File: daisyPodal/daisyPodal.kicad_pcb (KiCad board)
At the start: 2 copper layers, 76 x 86 mm, 45 parts, among them J1 Guitar in, J2 Left out, J3 fsw pin 1, J4 fsw pin 4, J5 fsw pin 6, J6 fsw pin 3, J7 fsw pin 2, J8 fsw pin 5, SW1 Switch 1, SW2 Switch 2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

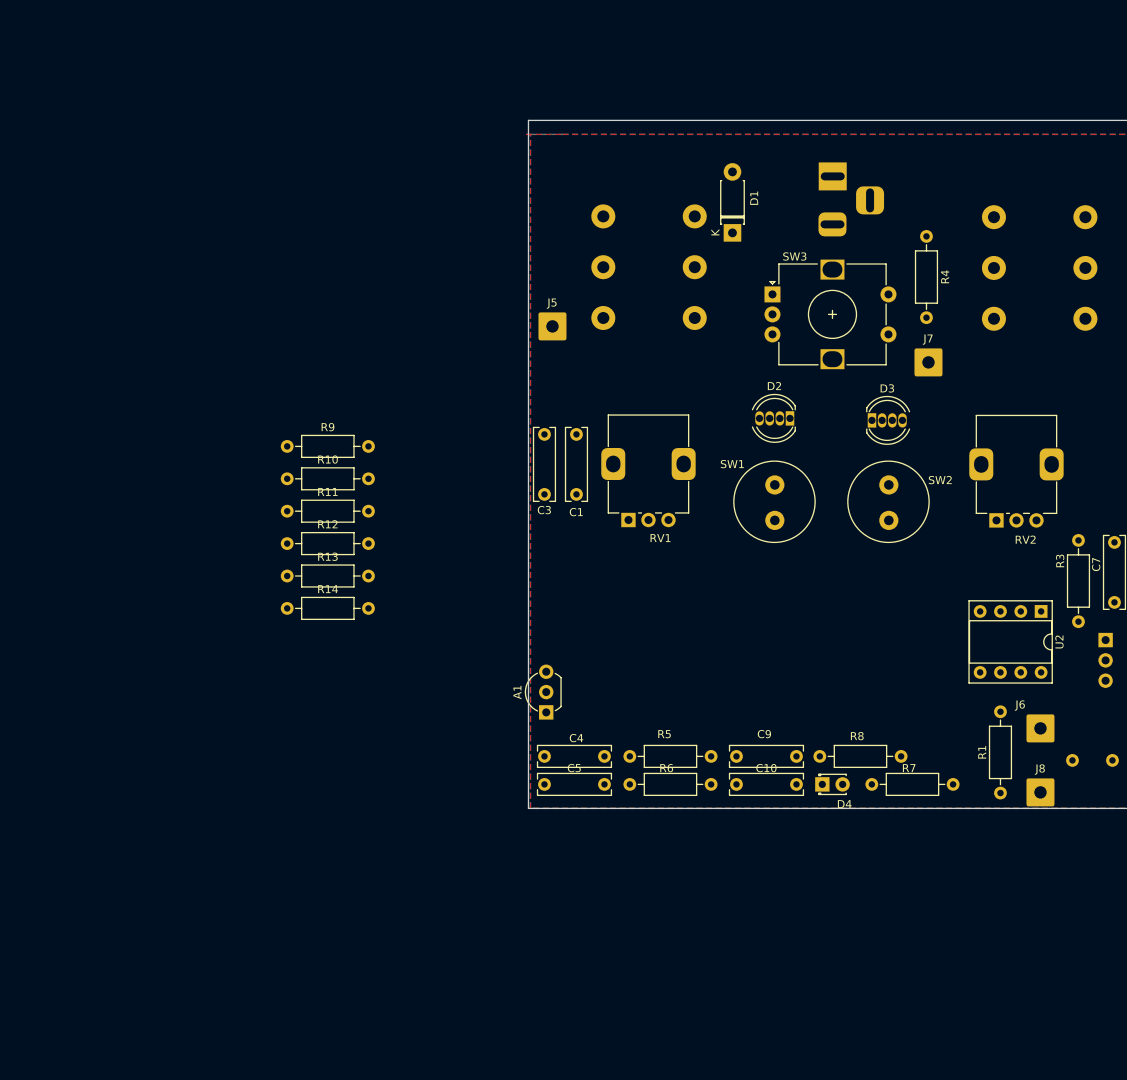
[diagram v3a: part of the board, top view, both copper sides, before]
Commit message: Add right out - stereo now
Replaced TL072 with TL074
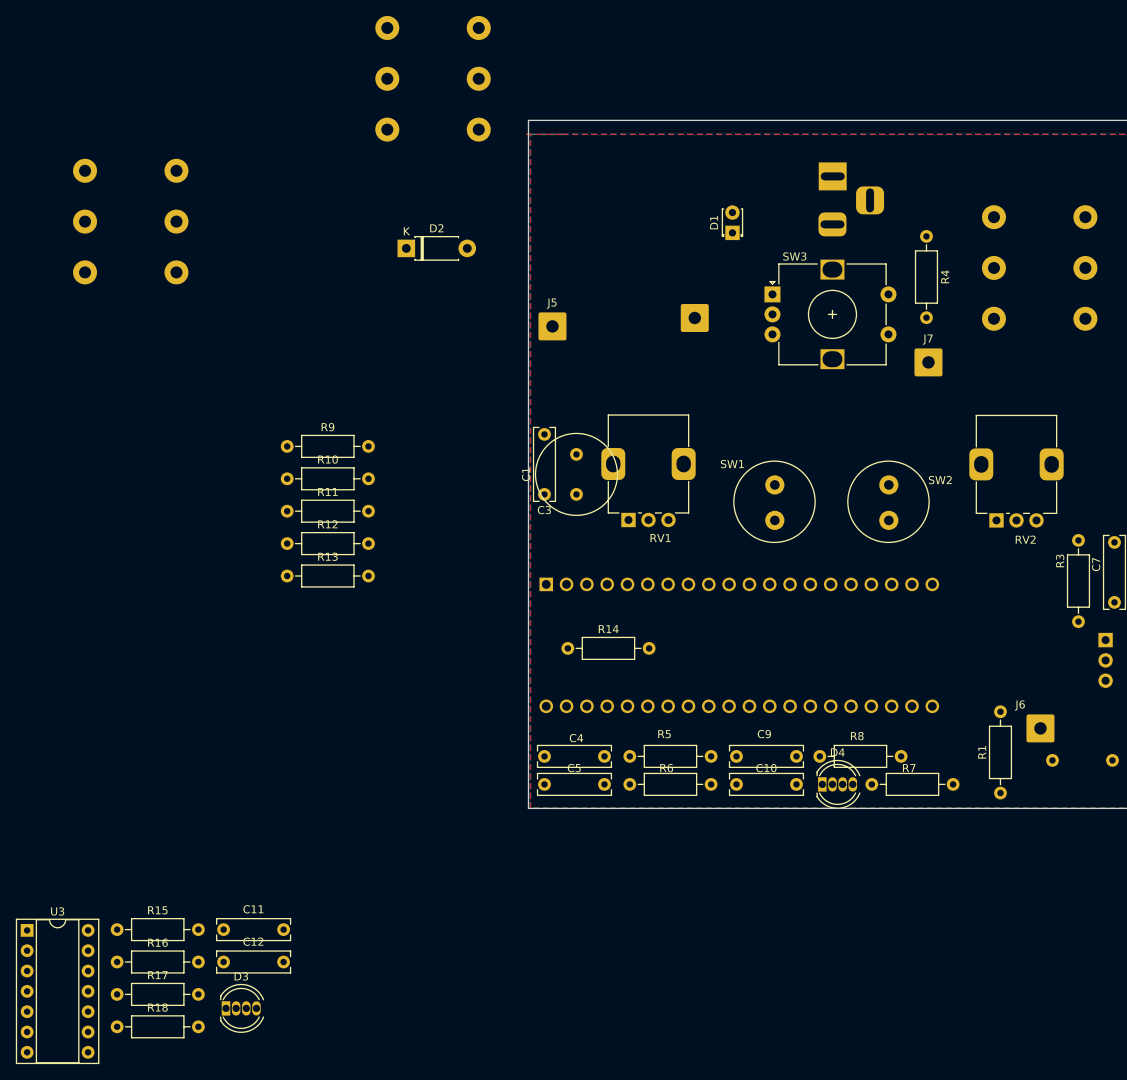
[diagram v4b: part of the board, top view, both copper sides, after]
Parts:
- removed U2: TL072, Package_DIP:DIP-8_W7.62mm_Socket
- added C11: 1u, Capacitor_THT:C_Rect_L9.0mm_W2.5mm_P7.50mm_MKT, F.Cu at (61.9, 137.2)
- added C12: 1u, Capacitor_THT:C_Rect_L9.0mm_W2.5mm_P7.50mm_MKT, F.Cu at (61.9, 141.2)
- added J10: Right out, Connector_Audio:Jack_6.35mm_Neutrik_NRJ6HM-1_Horizontal, B.Cu at (56.0, 55.0)
- added R15: 1M, Resistor_THT:R_Axial_DIN0207_L6.3mm_D2.5mm_P10.16mm_Horizontal, F.Cu at (48.6, 137.2)
- added R16: 1M, Resistor_THT:R_Axial_DIN0207_L6.3mm_D2.5mm_P10.16mm_Horizontal, F.Cu at (48.6, 141.2)
- added R17: 100R, Resistor_THT:R_Axial_DIN0207_L6.3mm_D2.5mm_P10.16mm_Horizontal, F.Cu at (48.6, 145.2)
- added R18: 100K, Resistor_THT:R_Axial_DIN0207_L6.3mm_D2.5mm_P10.16mm_Horizontal, F.Cu at (48.6, 149.3)
- added U3: TL074, Package_DIP:DIP-14_W7.62mm_Socket, F.Cu at (37.3, 137.2)
- A1: footprint Package_TO_SOT_THT:TO-92_Inline_Wide_78L05_dc -> Module:Electrosmith_Daisy_Seed; moved to B.Cu
- C1: value 100n -> 100u; footprint Capacitor_THT:C_Rect_L9.0mm_W2.5mm_P7.50mm_MKT -> Capacitor_THT:C_Radial_D10.0mm_H16.0mm_P5.00mm
- C2: value 100u -> 100p; footprint Capacitor_THT:C_Radial_D10.0mm_H16.0mm_P5.00mm -> Capacitor_THT:C_Rect_L9.0mm_W2.5mm_P7.50mm_MKT
- C3: value 100n -> 1u
- C6: value 100p -> 1n
- C7: value 1n -> 100n
- C8: value 1u -> 100n
- D1: value 1N5819 -> LED; footprint Diode_THT:D_DO-41_SOD81_P7.62mm_Horizontal -> LED_THT:LED_D1.8mm_W3.3mm_H2.4mm
- D2: value LED 1 -> 1N5819; footprint LED_THT:LED_D5.0mm-4_RGB -> Diode_THT:D_DO-41_SOD81_P7.62mm_Horizontal
- D3: value LED 2 -> LED_RAGB
- D4: value LED -> LED_RAGB; footprint LED_THT:LED_D1.8mm_W3.3mm_H2.4mm -> LED_THT:LED_D5.0mm-4_RGB
- J2: value Left out -> fsw pin 1; footprint Connector_Audio:Jack_6.35mm_Neutrik_NRJ6HM-1_Horizontal -> Connector_Wire:SolderWire-0.75sqmm_1x01_D1.25mm_OD3.5mm
- J3: value fsw pin 1 -> fsw pin 2
- J5: value fsw pin 6 -> fsw pin 5
- J6: value fsw pin 3 -> fsw pin 6
- J7: value fsw pin 2 -> fsw pin 3
- J8: value fsw pin 5 -> Left out; footprint Connector_Wire:SolderWire-0.75sqmm_1x01_D1.25mm_OD3.5mm -> Connector_Audio:Jack_6.35mm_Neutrik_NRJ6HM-1_Horizontal; moved to B.Cu
- R1, R2: value 1M -> 1k
- R13: value 1k -> 100R
- R14: value 1k -> 100K
- R3, R4: value 1k -> 1M
- R7: value 100K -> 1k
- R8: value 100R -> 1k
- SW1: value Switch 1 -> Switch 2
- SW2: value Switch 2 -> Switch 1
- moved D3 109.2 mm to (62.2, 147.0)
- moved J8 108.6 mm to (93.8, 37.1), turned to 90 degrees
- moved D2 52.5 mm to (84.7, 52.0), turned to 0 degrees
- moved R14 35.4 mm to (104.9, 102.0)
- moved A1 16.0 mm to (102.2, 94.0), turned to -90 degrees
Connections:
- C1 pad 1: GND -> /VCC
- C1 pad 2: /VCC -> GND
- C10 pad 1: /Left out -> Net-(C10-Pad1)
- C10 pad 2: Net-(U2B-+) -> Net-(J7-Pin_1)
- C2 pad 1: /VCC -> Net-(J4-Pin_1)
- C3 pad 1: GND -> Net-(J4-Pin_1)
- C3 pad 2: /VCC -> Net-(C3-Pad2)
- C4 pad 2: +5V -> /VCC
- C5 pad 2: +5V -> /VCC
- C6 pad 1: Net-(J4-Pin_1) -> Net-(U3A-+)
- C7 pad 1: Net-(U2A-+) -> GND
- C7 pad 2: GND -> +5V
- C8 pad 1: Net-(J4-Pin_1) -> GND
- C8 pad 2: Net-(C8-Pad2) -> +5V
- C9 pad 1: Net-(C9-Pad1) -> /Left out
- C9 pad 2: Net-(J6-Pin_1) -> Net-(U3B-+)
- D1 pad 1: /VCC -> Net-(D1-K)
- D1 pad 2: Net-(BT1-+) -> Net-(D1-A)
- D2 pad 1: /LED_1_G -> /VCC
- D2 pad 2: /LED_1_B -> Net-(BT1-+)
- D3 pad 1: /LED_2_G -> Net-(D3-RK)
- D3 pad 2: /LED_2_B -> /3v3
- D3 pad 3: GND -> Net-(D3-GK)
- D3 pad 4: /LED_2_R -> Net-(D3-BK)
- D4 pad 1: Net-(D4-K) -> Net-(D4-RK)
- D4 pad 2: Net-(D4-A) -> /3v3
- J1 pad T: Net-(J3-Pin_1) -> Net-(J2-Pin_1)
- J3 pad 1: Net-(J3-Pin_1) -> Net-(D1-K)
- J5 pad 1: Net-(J5-Pin_1) -> GND
- J7 pad 1: Net-(D4-K) -> Net-(J7-Pin_1)
- R1 pad 1: +5V -> Net-(BT1-+)
- R1 pad 2: Net-(U2A-+) -> Net-(D1-A)
- R10 pad 1: /LED_1_G -> /LED_2_B
- R10 pad 2: Net-(D7-GK) -> Net-(D4-RK)
- R11 pad 1: /LED_1_R -> /LED_2_G
- R11 pad 2: Net-(D7-BK) -> Net-(D4-GK)
- R12 pad 1: /LED_2_B -> /LED_2_R
- R12 pad 2: Net-(D2-RK) -> Net-(D4-BK)
- R13 pad 1: /LED_2_G -> Net-(U3B--)
- R13 pad 2: Net-(D2-GK) -> Net-(C10-Pad1)
- R14 pad 1: /LED_2_R -> Net-(J7-Pin_1)
- R14 pad 2: Net-(D2-BK) -> GND
- R2 pad 1: Net-(U2A-+) -> Net-(C3-Pad2)
- R2 pad 2: GND -> Net-(U3A-+)
- R3 pad 1: Net-(C8-Pad2) -> +5V
- R3 pad 2: Net-(U2A-+) -> Net-(U3A-+)
- R4 pad 1: Net-(BT1-+) -> Net-(U3A-+)
- R4 pad 2: Net-(D4-A) -> GND
- R5 pad 2: Net-(U2B-+) -> Net-(U3B-+)
- R6 pad 1: Net-(U2B-+) -> Net-(U3B-+)
- R7 pad 1: Net-(J6-Pin_1) -> /LED_1_B
- R7 pad 2: GND -> Net-(D3-RK)
- R8 pad 1: Net-(U2B--) -> /LED_1_G
- R8 pad 2: Net-(C9-Pad1) -> Net-(D3-GK)
- R9 pad 1: /LED_1_B -> /LED_1_R
- R9 pad 2: Net-(D7-RK) -> Net-(D3-BK)
- SW1 pad 1: Net-(A1-SAI2_FS) -> Net-(A1-SAI2_SCK)
- SW2 pad 1: Net-(A1-SAI2_SCK) -> Net-(A1-SAI2_FS)

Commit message: reduce size of box capacitors to fit caps we use
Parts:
- moved D1 151.2 mm to (29.0, 166.4)
- moved J2 145.0 mm to (265.5, 70.0)
- moved SW2 137.7 mm to (266.5, 150.9)
- moved J7 130.8 mm to (272.5, 112.0)
- moved R4 128.4 mm to (274.5, 80.9)
- moved SW1 117.6 mm to (46.0, 167.4)
- moved BT1 113.9 mm to (251.5, 39.0)
- moved RV1 108.7 mm to (221.0, 92.5)
- moved SW3 94.2 mm to (208.2, 111.0)
- moved D4 91.6 mm to (49.1, 145.5)
- moved C9 86.6 mm to (212.8, 150.5)
- moved J6 86.6 mm to (243.2, 147.0)
- moved R3 86.6 mm to (248.0, 123.5)
- moved R8 86.6 mm to (225.8, 150.5)
- moved RV2 86.6 mm to (237.8, 121.0)
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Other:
- board size 76 x 86 mm -> 76 x 80 mm

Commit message: Place components on PCB in sensible blocks
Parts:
- removed J10: Right out, Connector_Audio:Jack_6.35mm_Neutrik_NRJ6HM-1_Horizontal
- removed U3: TL074, Package_DIP:DIP-14_W7.62mm_Socket
- added J9: fsw pin 3, Connector_Wire:SolderWire-0.75sqmm_1x01_D1.25mm_OD3.5mm, F.Cu at (140.0, 55.0)
- added U2: TL074, Package_DIP:DIP-14_W7.62mm_Socket, F.Cu at (136.9, 106.0)
- C1: moved to B.Cu
- C10, C11, C12, C3, C4, C5, C6, C7, C8, C9: footprint Capacitor_THT:C_Rect_L9.0mm_W2.5mm_P7.50mm_MKT -> Capacitor_THT:C_Rect_L7.0mm_W2.5mm_P5.00mm
- C2: footprint Capacitor_THT:C_Rect_L9.0mm_W2.5mm_P7.50mm_MKT -> Capacitor_THT:C_Rect_L7.0mm_W2.5mm_P5.00mm; moved to F.Cu
- J2: moved to F.Cu
- J7: value fsw pin 3 -> Left out; footprint Connector_Wire:SolderWire-0.75sqmm_1x01_D1.25mm_OD3.5mm -> Connector_Audio:Jack_6.35mm_Neutrik_NRJ6HM-1_Horizontal; moved to B.Cu
- J8: value Left out -> Right out
- R13: value 100R -> 1k
- R14: value 100K -> 1k
- R15, R16: value 1M -> 100R
- R17: value 100R -> 100K
- R7, R8: value 1k -> 1M
- SW1: value Switch 2 -> Switch 1; footprint Button_Switch_THT:SW_CW_GPTS203211B_1 podal -> Connector_Wire:SolderWire-0.75sqmm_1x02_P7mm_D1.25mm_OD3.5mm
- SW2: value Switch 1 -> Switch 2; footprint Button_Switch_THT:SW_CW_GPTS203211B_1 podal -> Connector_Wire:SolderWire-0.75sqmm_1x02_P7mm_D1.25mm_OD3.5mm
- moved J5 153.8 mm to (172.0, 123.0)
- moved J7 146.0 mm to (131.0, 76.0), turned to 90 degrees
- moved J6 133.1 mm to (125.0, 86.0)
- moved D2 130.8 mm to (124.0, 129.0)
- moved J3 126.6 mm to (142.0, 130.0)
- moved D4 119.2 mm to (160.1, 102.0)
- moved R4 119.2 mm to (156.0, 67.8)
- moved R18 117.0 mm to (136.0, 65.0), turned to 90 degrees
- moved R8 115.4 mm to (136.0, 78.0), turned to 90 degrees
- moved D1 115.2 mm to (138.3, 130.0), turned to 180 degrees
- moved R16 114.5 mm to (142.0, 78.0), turned to 90 degrees
- moved R12 113.5 mm to (131.8, 115.0)
- moved SW2 111.7 mm to (157.0, 129.0)
- moved RV1 111.5 mm to (109.5, 95.0)
- moved R13 110.8 mm to (131.8, 118.0)
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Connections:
- C10 pad 1: Net-(C10-Pad1) -> /Left out
- C10 pad 2: Net-(J7-Pin_1) -> Net-(U2B-+)
- C11 pad 1: /Right out -> Net-(C11-Pad1)
- C11 pad 2: Net-(U3C-+) -> Net-(C11-Pad2)
- C6 pad 1: Net-(U3A-+) -> Net-(U2A-+)
- C9 pad 1: /Left out -> /Right out
- J8 pad T: Net-(J6-Pin_1) -> Net-(C11-Pad2)
- R10 pad 1: /LED_2_B -> /LED_1_G
- R10 pad 2: Net-(D4-RK) -> Net-(D3-GK)
- R11 pad 1: /LED_2_G -> /LED_1_R
- R11 pad 2: Net-(D4-GK) -> Net-(D3-BK)
- R12 pad 1: /LED_2_R -> /LED_2_B
- R12 pad 2: Net-(D4-BK) -> Net-(D4-RK)
- R13 pad 1: Net-(U3B--) -> /LED_2_G
- R13 pad 2: Net-(C10-Pad1) -> Net-(D4-GK)
- R14 pad 1: Net-(J7-Pin_1) -> /LED_2_R
- R14 pad 2: GND -> Net-(D4-BK)
- R15 pad 1: +5V -> Net-(U2C--)
- R15 pad 2: Net-(U3C-+) -> Net-(C11-Pad1)
- R16 pad 1: Net-(U3C-+) -> Net-(U2B--)
- R16 pad 2: GND -> Net-(C12-Pad1)
- R17 pad 1: Net-(U3C--) -> Net-(C11-Pad2)
- R17 pad 2: Net-(C12-Pad1) -> GND
- R2 pad 2: Net-(U3A-+) -> Net-(U2A-+)
- R3 pad 2: Net-(U3A-+) -> Net-(R3-Pad2)
- R4 pad 1: Net-(U3A-+) -> Net-(R3-Pad2)
- R7 pad 1: /LED_1_B -> +5V
- R7 pad 2: Net-(D3-RK) -> Net-(U2B-+)
- R8 pad 1: /LED_1_G -> Net-(U2B-+)
- R8 pad 2: Net-(D3-GK) -> GND
- R9 pad 1: /LED_1_R -> /LED_1_B
- R9 pad 2: Net-(D3-BK) -> Net-(D3-RK)
- SW1 pad 1: Net-(A1-SAI2_SCK) -> Net-(A1-SAI2_FS)
- SW2 pad 1: Net-(A1-SAI2_FS) -> Net-(A1-SAI2_SCK)
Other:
- board text added: "Podal v0.2 Denis Crowdy"
- board text removed: "Podal v0.1"

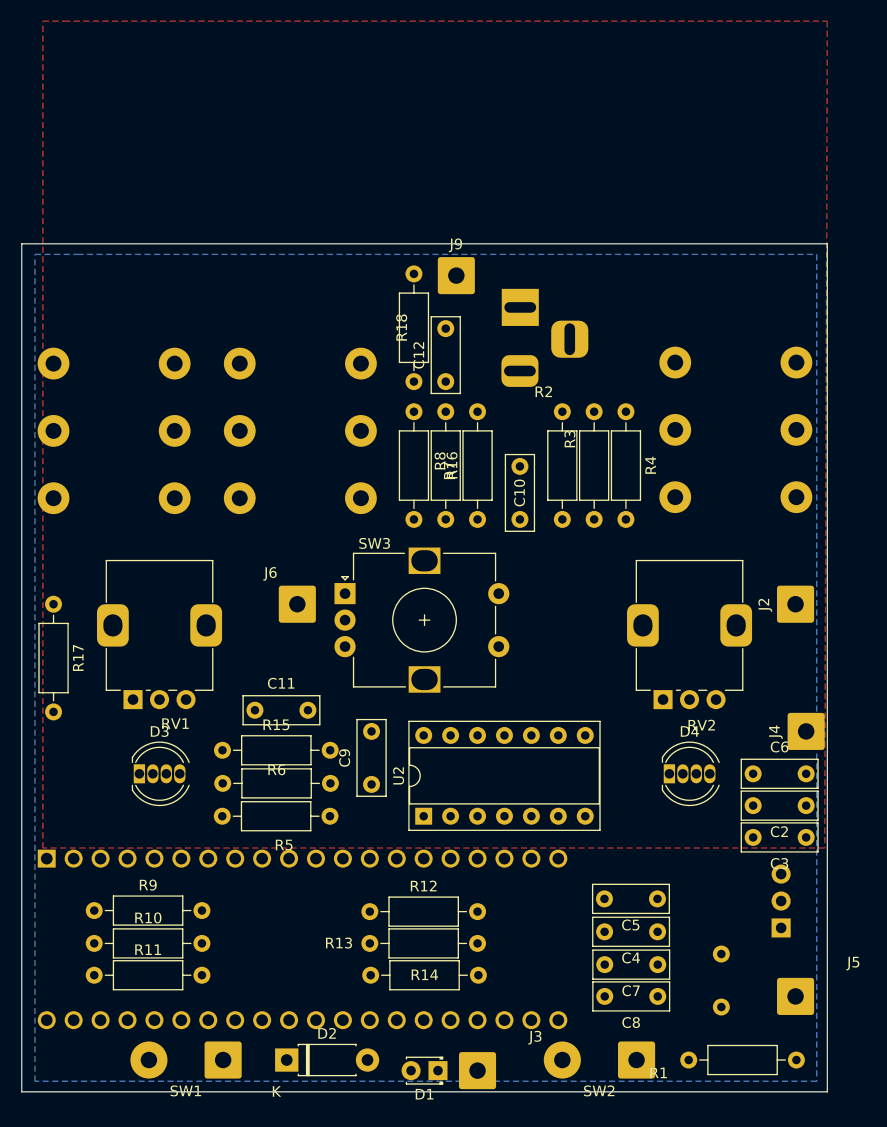
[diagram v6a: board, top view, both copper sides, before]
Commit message: Connect everything together on PCB
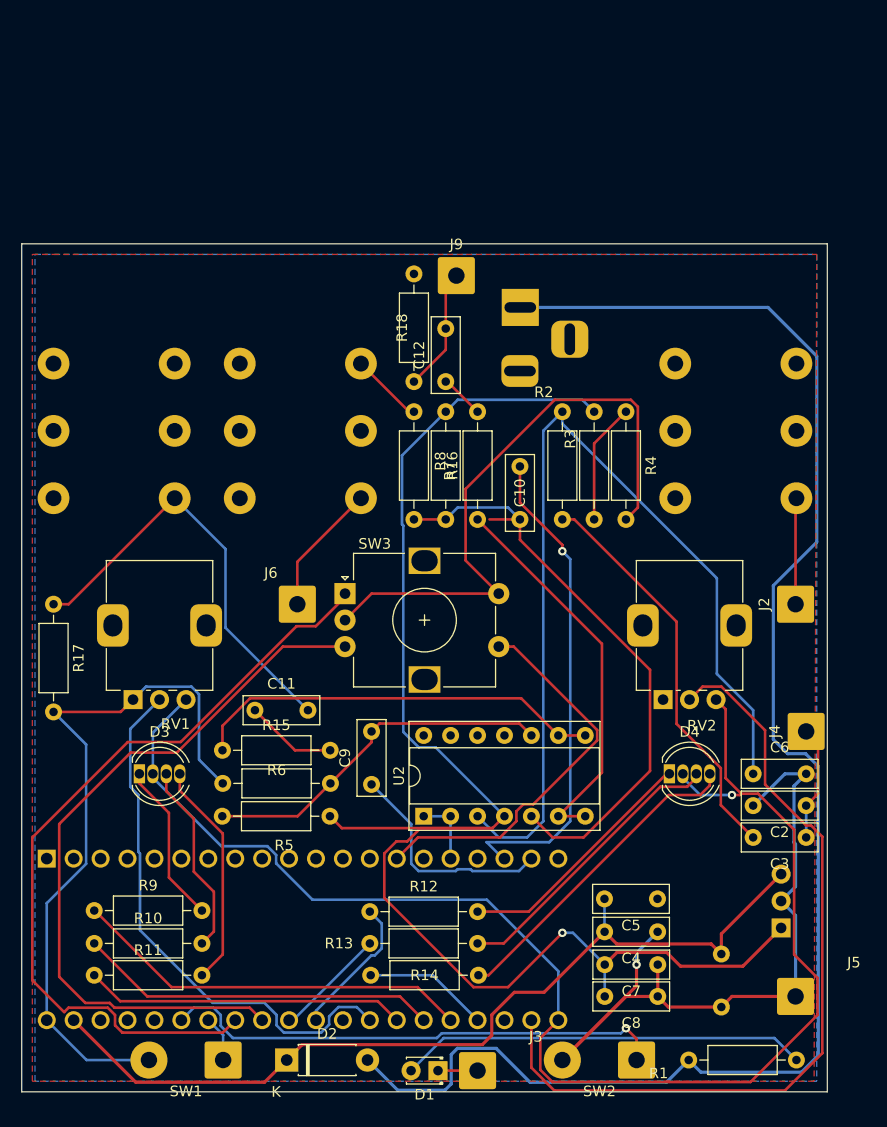
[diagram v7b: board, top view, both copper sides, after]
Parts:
- moved J1 0.10 mm to (172.1, 76.0)
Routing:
- net GND: track 0.00 -> 205.4 mm, vias 0 -> 1
- net Net-(BT1-+): track 0.00 -> 150.6 mm
- net +5V: track 0.00 -> 142.3 mm, vias 0 -> 1
- net /3v3: track 0.00 -> 135.4 mm, vias 0 -> 1
- net Net-(U2A-+): track 0.00 -> 88.7 mm
- net /VCC: track 0.00 -> 84.4 mm
- net Net-(A1-ADC_0): track 0.00 -> 76.6 mm
- net Net-(A1-SAI2_SD_A): track 0.00 -> 75.3 mm
- net Net-(A1-SAI2_SD_B): track 0.00 -> 69.1 mm
- net Net-(U2B-+): track 0.00 -> 57.2 mm
- net Net-(A1-ADC_6): track 0.00 -> 51.5 mm
- net Net-(A1-SAI2_SCK): track 0.00 -> 48.0 mm, vias 0 -> 1
- net /Left out: track 0.00 -> 47.4 mm, vias 0 -> 1
- net Net-(C11-Pad2): track 0.00 -> 40.8 mm
- net Net-(U2C--): track 0.00 -> 39.1 mm
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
